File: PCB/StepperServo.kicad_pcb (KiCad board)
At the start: 2 copper layers, 56 x 56 mm, 74 parts, among them P1 Conn_01x06, P2 Conn_01x04, P4 Conn_01x08, P5 Conn_01x02, U2 A4950E, U3 EL-0631, U4 A4950E, U6 EL357NC, U7 STM32F103CBTx, U9 PCA82C251, p7 Conn_01x08

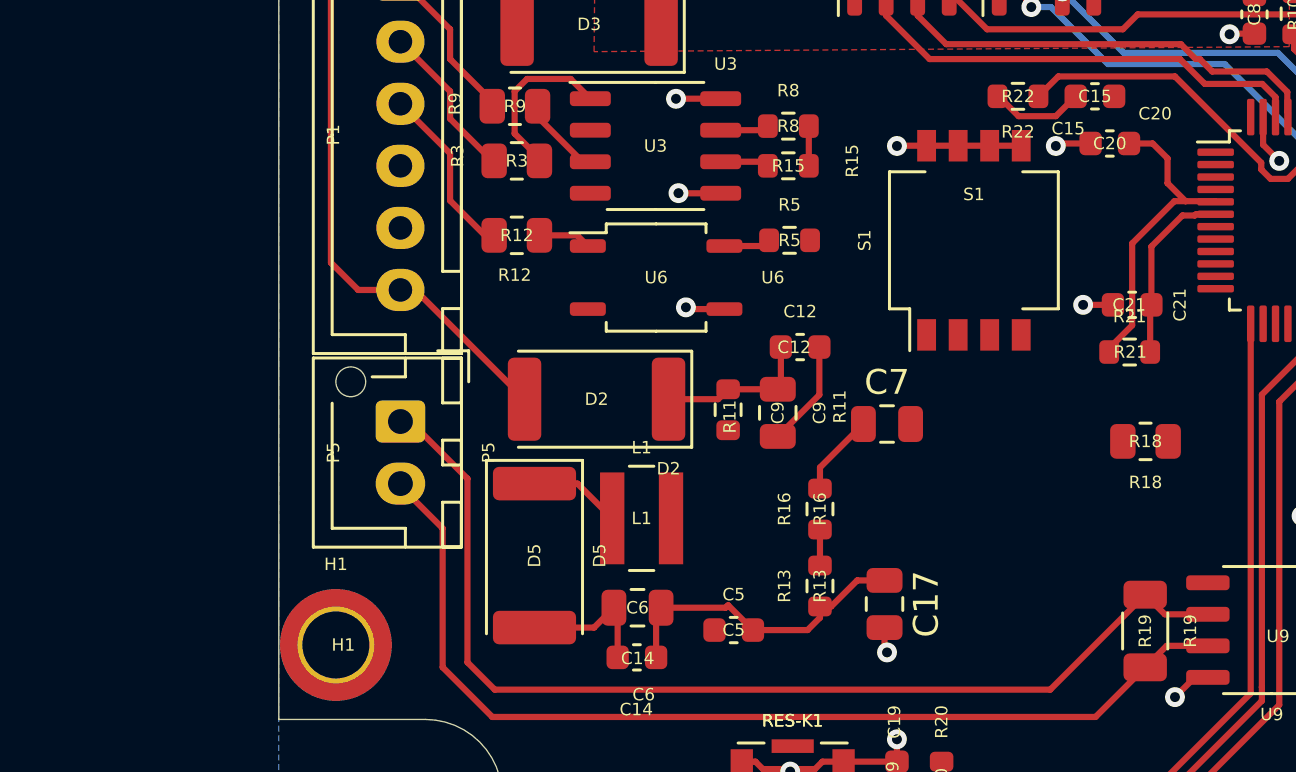
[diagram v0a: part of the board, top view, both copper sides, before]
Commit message: Added misssing footprints to pcb
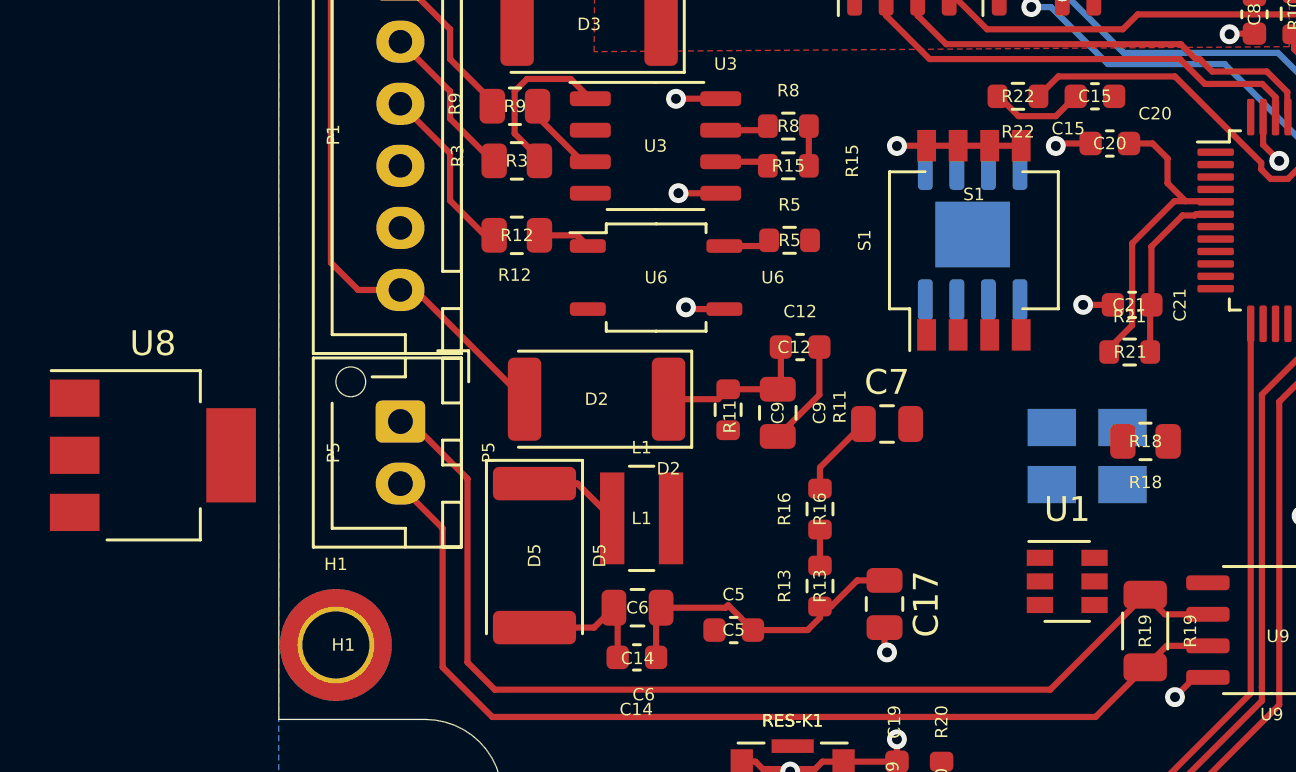
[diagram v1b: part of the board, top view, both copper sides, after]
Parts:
- added U1: BNOR11, Package_TO_SOT_SMD:SOT-23-6, F.Cu at (111.8, 91.4)
- added U5: TLE5012B, Package_SO:Infineon_PG-DSO-8-27_3.9x4.9mm_EP2.65x3mm, B.Cu at (108.0, 77.5)
- added U8: LD1117S33CTR, Package_TO_SOT_SMD:SOT-223, F.Cu at (74.9, 86.4)
- added Y1: Crystal, Crystal:Crystal_SMD_EuroQuartz_MT-4Pin_3.2x2.5mm_HandSoldering, B.Cu at (112.6, 86.4)
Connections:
- C15 pad 1: +3V3 -> VDD
- C7 pad 2: +3V3 -> VDD
- P1 pad 5: Net-(P1-Pad5) -> com
- P4 pad 2: +3V3 -> VDD
- P4 pad 5: +3V3 -> VDD
- R14 pad 1: +3V3 -> VDD
- U3 pad 1: Net-(R3-Pad1) -> com
- U3 pad 2: Net-(U3-Pad2) -> Net-(R3-Pad1)
- U3 pad 4: Net-(U3-Pad4) -> com
- U3 pad 8: VSS -> VDD
- U6 pad 1: Net-(R12-Pad1) -> com
- U6 pad 2: Net-(U6-Pad2) -> Net-(R12-Pad1)
- U7 pad 10: Net-(R8-Pad1) -> Net-(R15-Pad1)
- U7 pad 11: Net-(R15-Pad1) -> Net-(R8-Pad1)
- p7 pad 2: +3V3 -> Net-(p7-Pad2)
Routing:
- net VSS: track 68.0 -> 66.2 mm, vias 29 -> 28
- net VDD: track 11.7 -> 13.5 mm, vias 0 -> 1

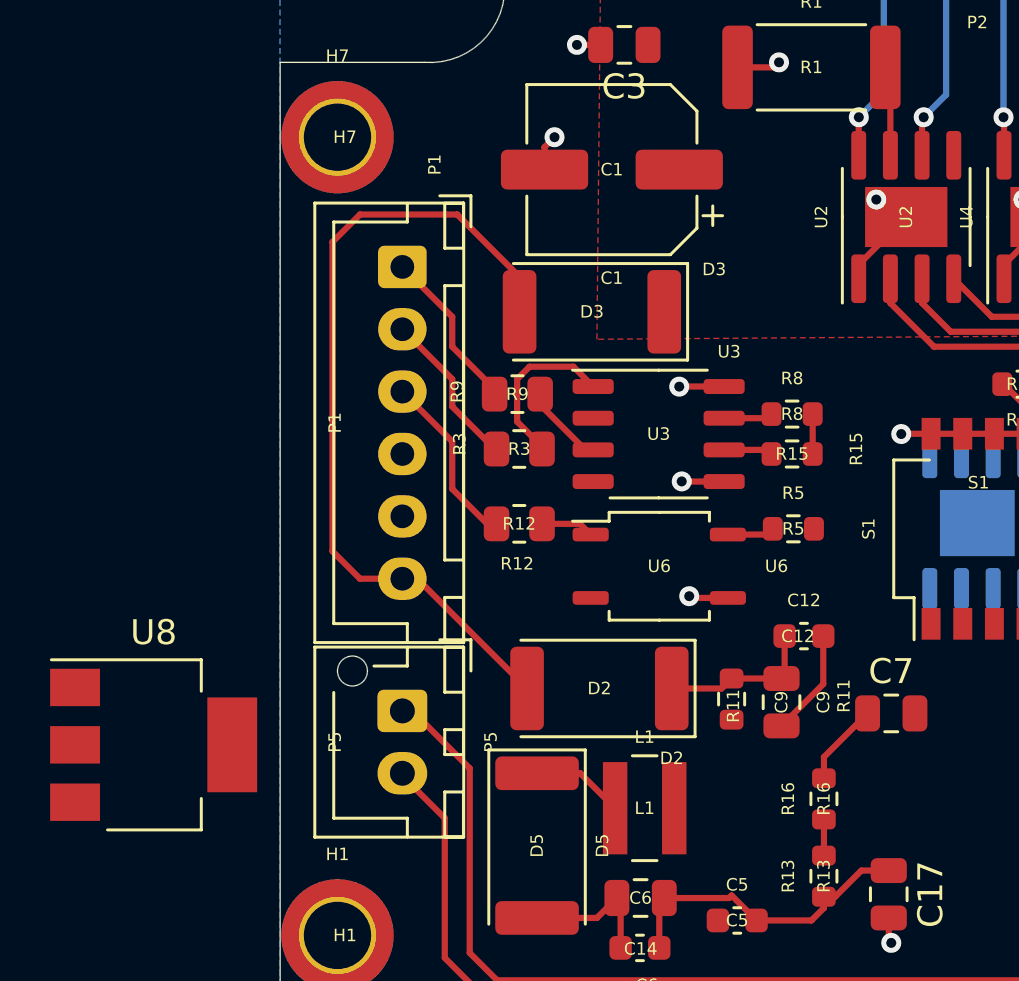
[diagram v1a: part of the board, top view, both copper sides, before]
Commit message: Removed dir, step, enable
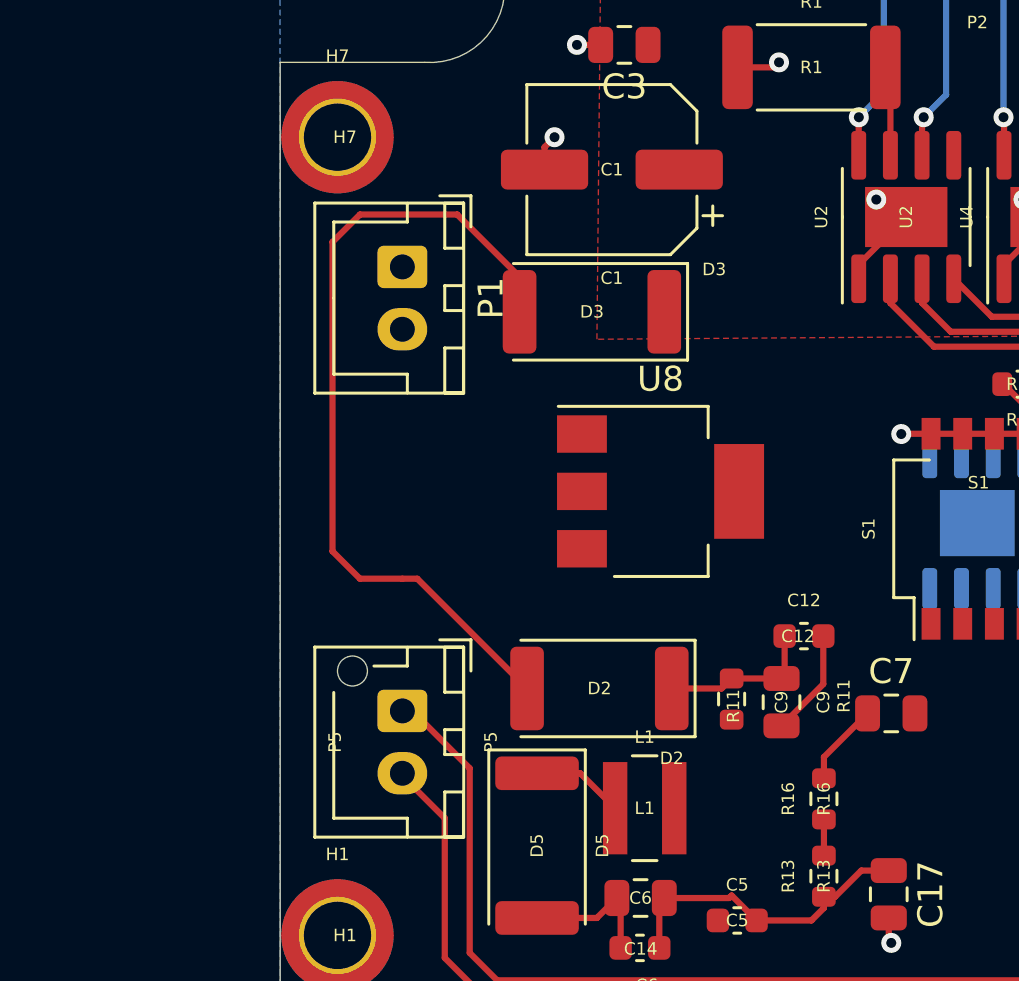
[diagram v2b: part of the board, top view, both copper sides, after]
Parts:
- removed R12, R3, R9: ?R, Resistor_SMD:R_0805_2012Metric
- removed R15, R5, R8: ?R, Resistor_SMD:R_0603_1608Metric
- removed U3: EL-0631, Package_SO:SOP-8_3.9x4.9mm_P1.27mm
- removed U6: EL357NC, Package_SO:SOP-4_3.8x4.1mm_P2.54mm
- P1: footprint Connector_JST:JST_XH_B6B-XH-A_1x06_P2.50mm_Vertical -> Connector_JST:JST_XH_B2B-XH-A_1x02_P2.50mm_Vertical
- moved U8 22.7 mm to (95.2, 76.2)
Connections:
- P1 pad 1: DIR_IN -> VSS
- P1 pad 2: STP_IN -> VMOT
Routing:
- net EN_IN: track 7.08 -> 0.00 mm
- net Net-(R3-Pad1): track 6.80 -> 0.00 mm
- net DIR_IN: track 6.63 -> 0.00 mm
- net STP_IN: track 6.41 -> 0.00 mm
- net VDD: track 13.5 -> 10.1 mm, vias 1 -> 0
- net Net-(R9-Pad1): track 3.30 -> 0.00 mm
- net VSS: track 66.2 -> 62.9 mm, vias 28 -> 26
- net Net-(R12-Pad1): track 2.13 -> 0.00 mm
- net Net-(U7-Pad11): track 1.97 -> 0.00 mm
- net Net-(U7-Pad10): track 1.97 -> 0.00 mm
- net Net-(U7-Pad12): track 1.90 -> 0.00 mm

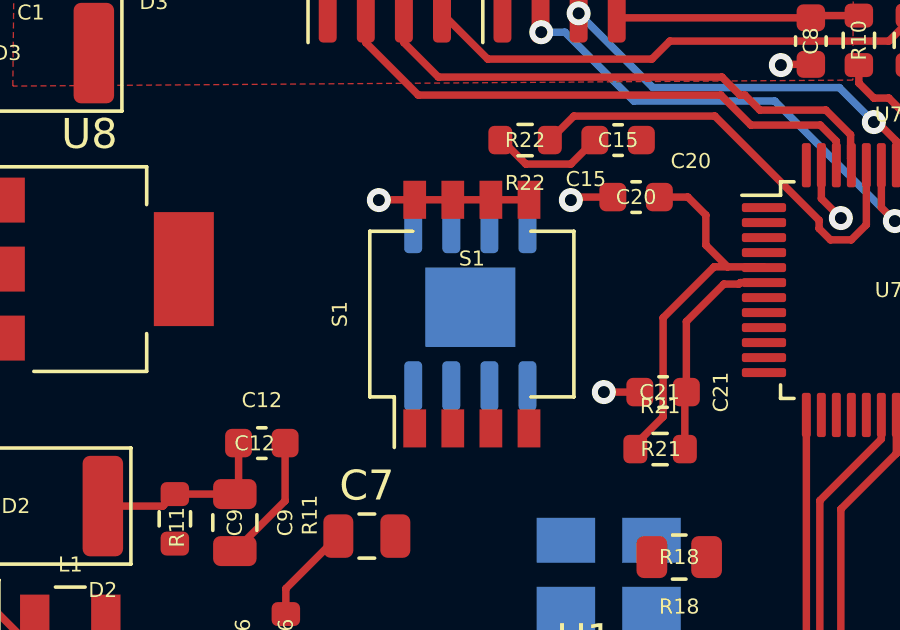
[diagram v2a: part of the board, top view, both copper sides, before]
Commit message: Removed dip switches
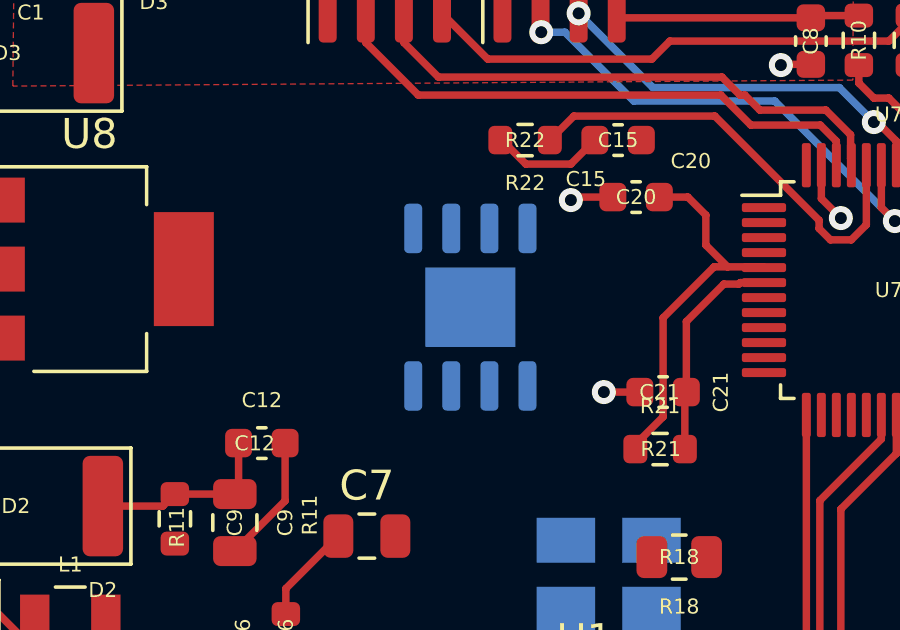
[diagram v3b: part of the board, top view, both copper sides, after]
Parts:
- removed S1: SW_DIP_x04, Button_Switch_SMD:SW_DIP_SPSTx04_Slide_KingTek_DSHP04TS_W7.62mm_P1.27mm
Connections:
- U7 pad 21: MICROSTEP1_SW -> Net-(U7-Pad21)
- U7 pad 22: MICROSTEP2_SW -> Net-(U7-Pad22)
- U7 pad 38: CALIB_SWITCH -> Net-(U7-Pad38)
- U7 pad 39: CLOSED_LOOP_SW -> Net-(U7-Pad39)
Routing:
- net VSS: track 62.9 -> 57.9 mm, vias 26 -> 25

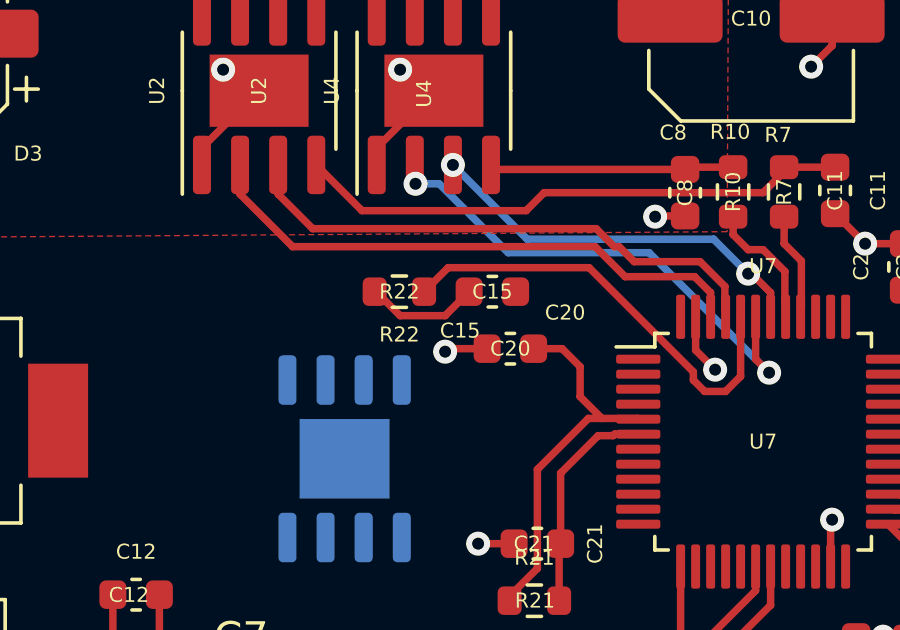
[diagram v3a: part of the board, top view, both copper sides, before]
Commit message: Boot0 to gnd
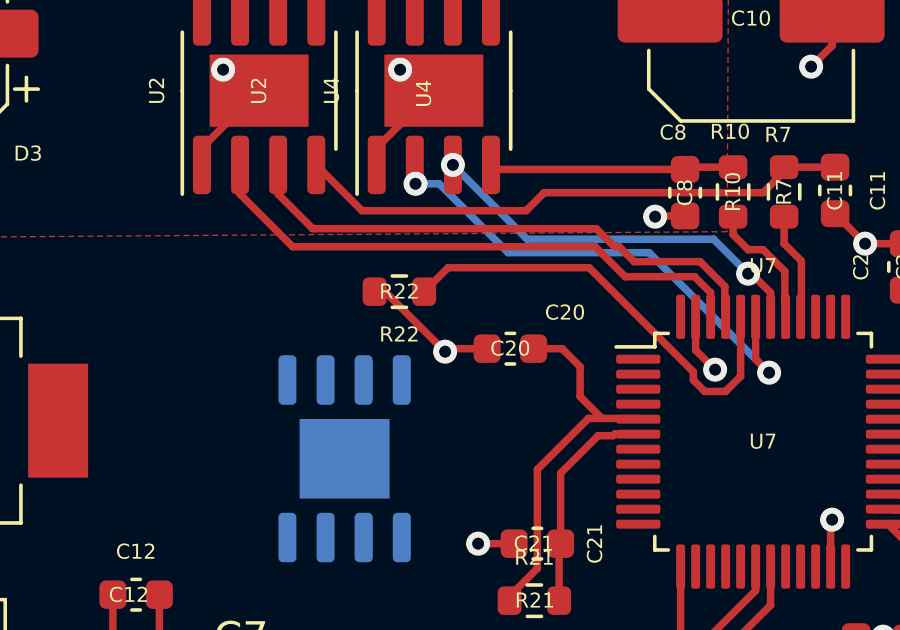
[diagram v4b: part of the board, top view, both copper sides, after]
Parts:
- removed C15: C, Capacitor_SMD:C_0603_1608Metric
- R22: value ?R -> 10k
- U1: value BNOR11 -> AOZ1282CI
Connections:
- net error renamed Net-(D4-Pad2)
- R22 pad 2: Net-(C15-Pad2) -> VSS
- p7 pad 2: Net-(p7-Pad2) -> VDD
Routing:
- net VDD: track 10.1 -> 14.5 mm
- net +3V3: track 4.40 -> 0.00 mm
- net Net-(C15-Pad2): track 3.81 -> 0.00 mm
- net VSS: track 57.9 -> 61.1 mm

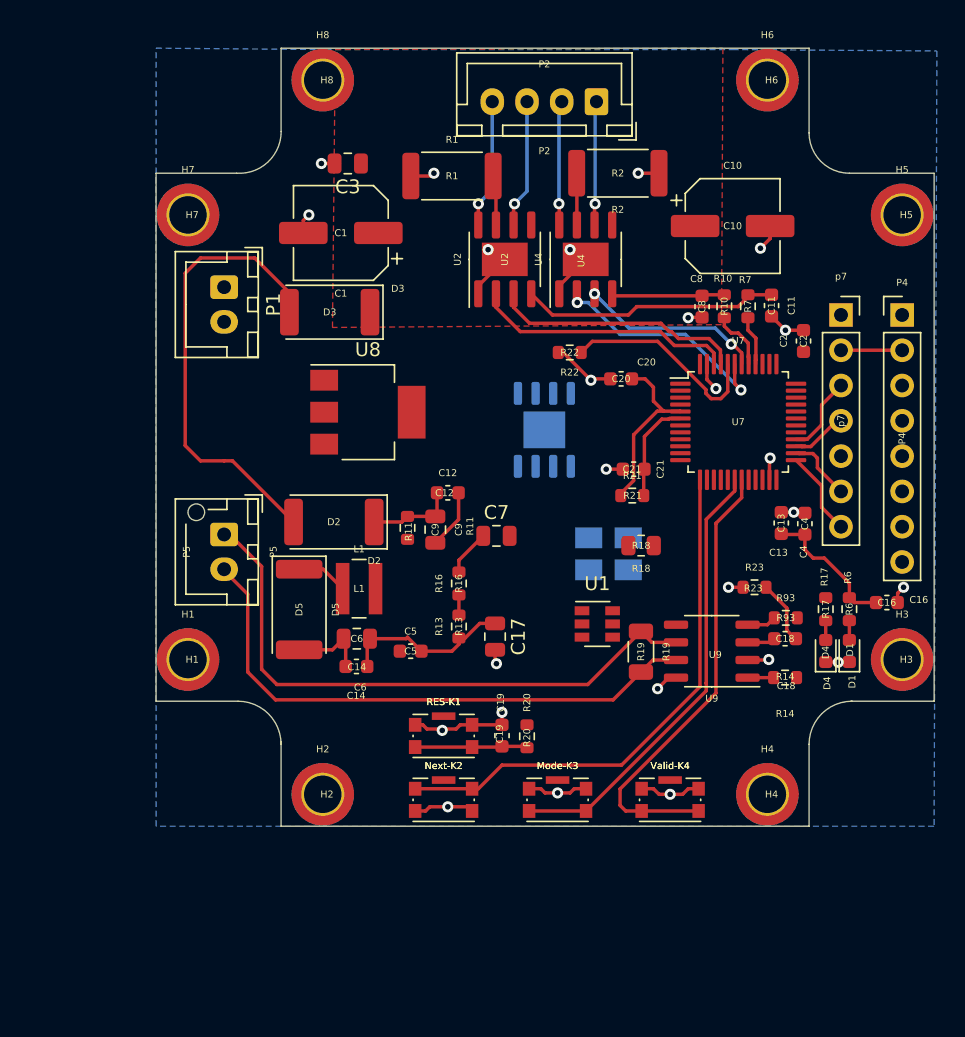
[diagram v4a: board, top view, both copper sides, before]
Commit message: NRST pull'up most likely not needed - set to virtual. A bit of cleanup.
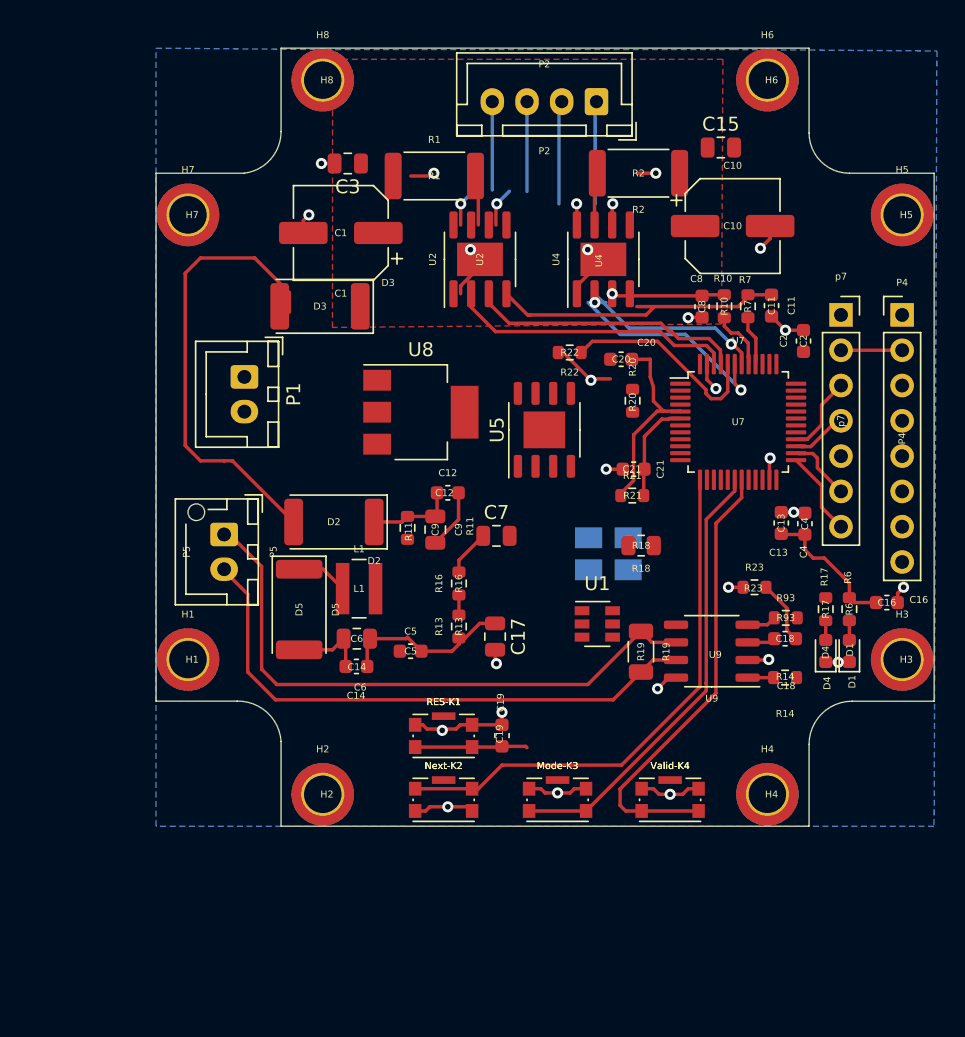
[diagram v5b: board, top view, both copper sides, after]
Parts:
- added C15: 0.22uF, Capacitor_SMD:C_0805_2012Metric, F.Cu at (120.7, 57.1)
- C19: value C -> 100nF
- C3: value C -> 0.22uF
- U5: moved to F.Cu
- moved R20 25.3 mm to (114.3, 75.4)
- moved P1 6.62 mm to (86.4, 73.7)
- moved U8 3.81 mm to (99.1, 76.2)
- moved U2 1.78 mm to (103.3, 65.2)
- moved R2 1.48 mm to (114.7, 59.0)
- moved C20 1.41 mm to (113.5, 72.4)
- moved R1 1.27 mm to (100.0, 59.2)
- moved U4 1.27 mm to (112.2, 65.2)
- moved D3 0.82 mm to (91.8, 68.6)
- turned U5 to 90 degrees
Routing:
- net motordriverU2#PWM: track 18.6 -> 21.7 mm
- net motordriverU2#2: track 18.8 -> 20.6 mm
- net motordriverU2#3: track 18.2 -> 19.8 mm
- net Net-(C20-Pad1): track 12.7 -> 14.2 mm
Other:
- outline, holes or cut-outs redrawn

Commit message: Kicad 6
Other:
- net class Default removed

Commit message: Clean
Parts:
- added P3: Conn_01x04, Connector_JST:JST_XH_B4B-XH-A_1x04_P2.50mm_Vertical, F.Cu at (106.7, 115.6)
- C1, C10: value 100 35V VT -> 100uF 35V VT
- Mode-K3, Next-K2, RES-K1, Valid-K4: footprint Button_Switch_SMD:SW_Push_1P1T-SH_NO_CK_KMR2xxG -> Button_Switch_SMD:SW_SPST_TL3342
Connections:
- U5 pad 1: Net-(U5-Pad1) -> unconnected-(U5-Pad1)
- U5 pad 5: Net-(U5-Pad5) -> unconnected-(U5-Pad5)
- U5 pad 8: Net-(U5-Pad8) -> unconnected-(U5-Pad8)
- U7 pad 10: Net-(U7-Pad10) -> unconnected-(U7-Pad10)
- U7 pad 11: Net-(U7-Pad11) -> unconnected-(U7-Pad11)
- U7 pad 12: Net-(U7-Pad12) -> unconnected-(U7-Pad12)
- U7 pad 21: Net-(U7-Pad21) -> unconnected-(U7-Pad21)
- U7 pad 22: Net-(U7-Pad22) -> unconnected-(U7-Pad22)
- U7 pad 3: Net-(U7-Pad3) -> unconnected-(U7-Pad3)
- U7 pad 38: Net-(U7-Pad38) -> unconnected-(U7-Pad38)
- U7 pad 39: Net-(U7-Pad39) -> unconnected-(U7-Pad39)
- U7 pad 4: Net-(U7-Pad4) -> unconnected-(U7-Pad4)
- U9 pad 5: Net-(U9-Pad5) -> unconnected-(U9-Pad5)
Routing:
- net VSS: track 61.1 -> 160.2 mm, vias 25 -> 24
- net Net-(Next-K2-Pad1): track 38.4 -> 0.00 mm
- net Net-(U7-Pad19): track 32.9 -> 0.00 mm
- net Net-(Mode-K3-Pad2): track 32.6 -> 0.00 mm
- net motordriverU4#3: track 13.2 -> 0.00 mm, vias 2 -> 0
- net motordriverU4#2: track 17.1 -> 30.2 mm, vias 2 -> 3
- net motordriverU2#2: track 20.6 -> 25.4 mm, vias 0 -> 1
- net motordriverU4#PWM: vias 0 -> 1
